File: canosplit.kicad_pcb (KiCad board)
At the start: 2 copper layers, 30 x 30 mm, 12 parts, among them J1 In, J2 Out, J3 Branch, J4 Power in

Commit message: researched parts
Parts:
- removed the REF** at (6.25, 5.75)
- J1, J2, J3: footprint Connector_Molex:Molex_PicoBlade_53398-0471_1x04-1MP_P1.25mm_Vertical -> Connector_Molex:Molex_PicoBlade_53047-0410_1x04_P1.25mm_Vertical
- J4: footprint Connector_Molex:Molex_PicoBlade_53398-0271_1x02-1MP_P1.25mm_Vertical -> Connector_Molex:Molex_PicoBlade_53047-0210_1x02_P1.25mm_Vertical
- moved J2 2.13 mm to (17.0, 26.2)
- moved J3 1.99 mm to (16.9, 15.0)
- moved J1 1.87 mm to (16.9, 3.80)
- moved J4 0.66 mm to (3.56, 9.67)
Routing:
- net /CAN_L: track 23.7 -> 41.9 mm
- net /CAN_H: track 23.0 -> 24.2 mm
- net +36V: track 33.6 -> 34.4 mm

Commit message: updated after meeting
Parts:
- removed JP2: Termination, Jumper:SolderJumper-2_P1.3mm_Open_TrianglePad1.0x1.5mm
- removed R2: 120R, Resistor_SMD:R_0805_2012Metric
- JP1: footprint Jumper:SolderJumper-2_P1.3mm_Open_TrianglePad1.0x1.5mm -> Connector_PinHeader_2.54mm:PinHeader_1x03_P2.54mm_Vertical
- moved G*** 15.1 mm to (22.2, 12.8)
- moved R1 1.25 mm to (14.4, 11.6)
- moved JP1 0.83 mm to (14.3, 8.60), turned to -90 degrees
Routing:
- net Net-(JP2-Pad2): track 2.77 -> 0.00 mm
- net +36V: track 34.4 -> 31.9 mm
- net /CAN_H: track 24.2 -> 22.6 mm
- net Net-(JP1-Pad2): track 2.38 -> 3.68 mm
- net GND: vias 52 -> 53

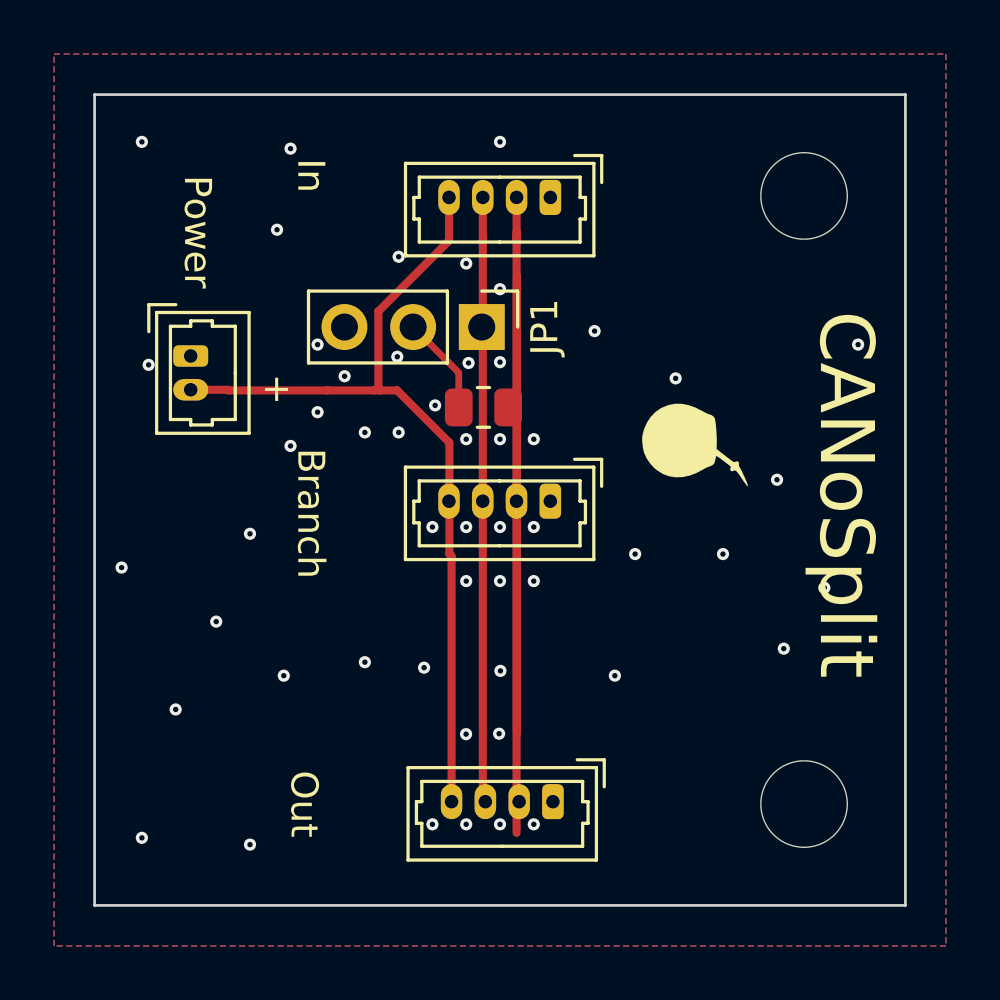
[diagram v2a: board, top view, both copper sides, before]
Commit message: updated board with new connector
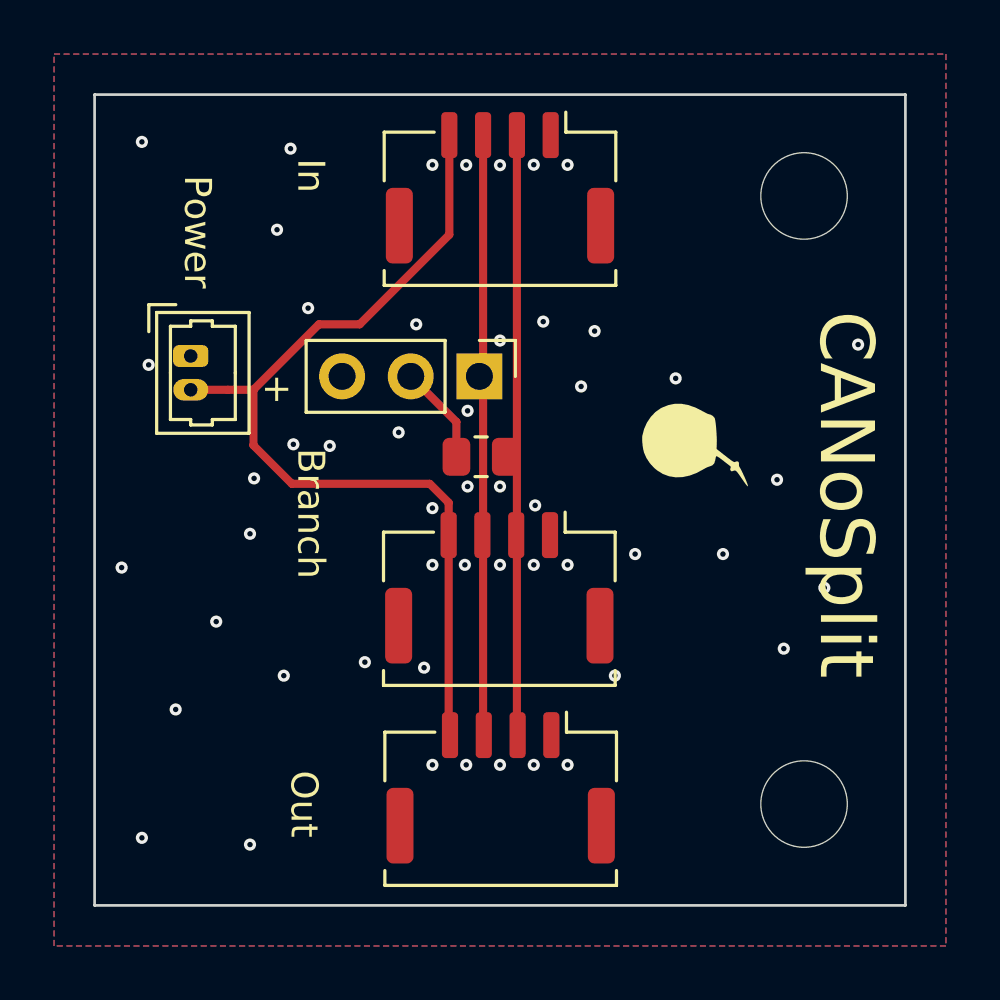
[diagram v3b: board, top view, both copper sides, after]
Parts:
- J1, J2, J3: footprint Connector_Molex:Molex_PicoBlade_53047-0410_1x04_P1.25mm_Vertical -> Connector_Molex:Molex_CLIK-Mate_502382-0470_1x04-1MP_P1.25mm_Vertical
- moved J3 3.72 mm to (15.0, 18.2)
- moved J2 2.00 mm to (15.0, 25.6)
- moved J1 1.90 mm to (15.0, 3.45)
- moved JP1 1.83 mm to (14.2, 10.4)
- moved R1 1.83 mm to (14.3, 13.4)
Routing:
- net /CAN_L: track 41.5 -> 22.2 mm
- net +36V: track 31.9 -> 34.4 mm
- net GND: vias 53 -> 51

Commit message: updated logo and text
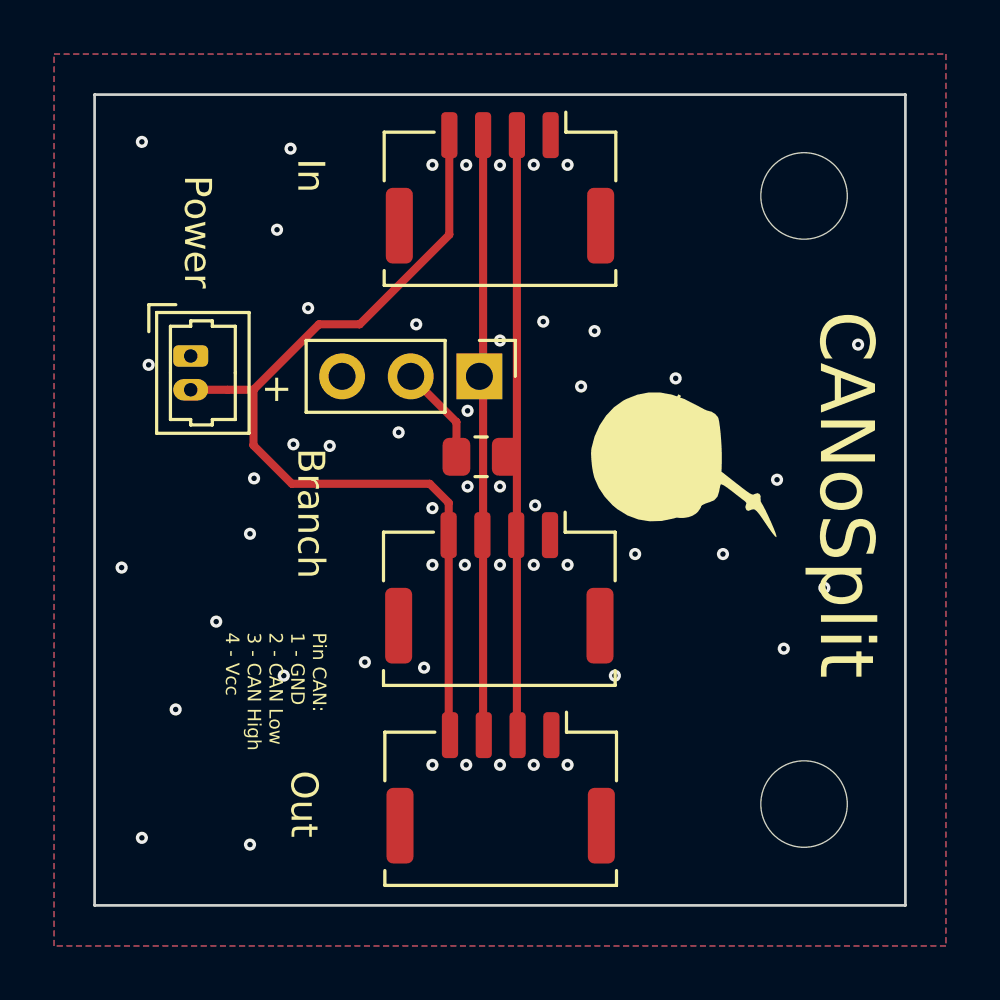
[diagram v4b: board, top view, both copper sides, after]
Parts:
- added REF**: OSHW-Logo2_7.3x6mm_SilkScreen, Symbol:OSHW-Logo2_7.3x6mm_SilkScreen, B.Cu at (5.50, 22.9)
- G***: footprint ownLib:ownLogoNew -> ownLib:LogoMate7x7
- moved G*** 0.74 mm to (21.8, 13.4)

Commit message: updated project
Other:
- outline, holes or cut-outs redrawn
- board text added: "V1"
- board text removed: "JLCJLCJLCJLC"
